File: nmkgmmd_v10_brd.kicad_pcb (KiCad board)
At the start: 2 copper layers, 85 x 69 mm, 155 parts, among them J1 CONN_01X05, J10 CONN_01X10, J14 CONN_01X10, J15 CONN_01X01, J16 CONN_01X01, J17 CONN_01X01, J18 CONN_01X01, J2 CONN_01X03, J20 CONN_01X10, J21 CONN_01X01, J22 CONN_01X01, J23 CONN_01X01, J24 CONN_01X01, J3 CONN_01X03, J4 CONN_01X04, J5 CONN_01X04, J6 CONN_01X04, J7 CONN_01X03, J8 CONN_01X03, J9 CONN_01X10, Q1 BSS138, Q10 PSMN1R0-40YLD, Q11 PSMN1R0-40YLD, Q12 PSMN1R0-40YLD, Q13 PSMN1R0-40YLD, Q14 PSMN1R0-40YLD, Q15 PSMN1R0-40YLD, Q16 PSMN1R0-40YLD, Q17 PSMN1R0-40YLD, Q18 BSS138, Q2 PSMN1R0-40YLD, Q3 PSMN1R0-40YLD, Q4 PSMN1R0-40YLD, Q5 PSMN1R0-40YLD, Q6 PSMN1R0-40YLD, Q7 PSMN1R0-40YLD, Q8 PSMN1R0-40YLD, Q9 PSMN1R0-40YLD, SW1 SKRPACE010, SW2 SW_DPDT_x2, U1 STM32F303CCTx, U2 MCP16301, U3 MCP16301, U4 A4957, U5 ACS711, U6 A4957, U7 ACS711, Y1 Crystal

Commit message: 進捗
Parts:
- moved C35 21.7 mm to (132.7, 106.7), turned to 0 degrees
- moved C33 18.5 mm to (132.7, 109.3), turned to 0 degrees
- moved C34 17.9 mm to (132.7, 108.0), turned to 0 degrees
- moved C37 2.02 mm to (132.7, 72.0)
- moved C36 1.33 mm to (132.7, 73.3)
- moved C38 0.76 mm to (132.7, 70.7)
- moved C31 0.76 mm to (126.7, 57.7)
- moved C23 0.56 mm to (124.5, 57.8)
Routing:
- net GND: track 552.0 -> 681.5 mm, vias 132 -> 162
- net V_BATT: track 209.9 -> 328.9 mm
- net (no net): track 1.40 -> 38.6 mm, vias 0 -> 10
- net +3V3: track 178.1 -> 210.4 mm, vias 7 -> 8
- net Net-(C22-Pad2): track 0.00 -> 32.2 mm, vias 0 -> 2
- net Net-(C21-Pad2): track 0.00 -> 16.9 mm, vias 0 -> 2
- net Net-(C31-Pad1): track 0.00 -> 9.49 mm, vias 0 -> 1
- net Net-(J18-Pad1): track 0.00 -> 6.72 mm
- net Net-(C20-Pad2): track 0.00 -> 2.65 mm, vias 0 -> 1

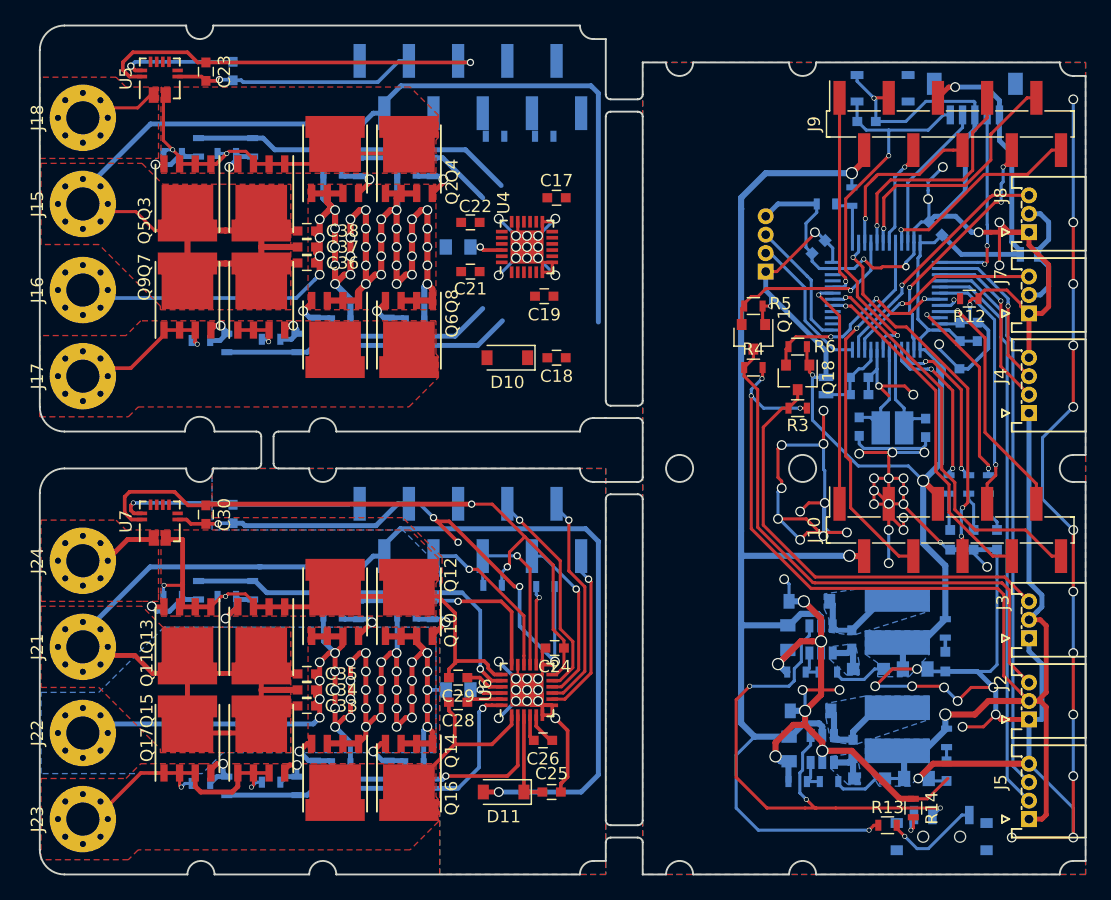
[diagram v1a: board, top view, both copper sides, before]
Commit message: 塗り忘れのviaがあったから塗った
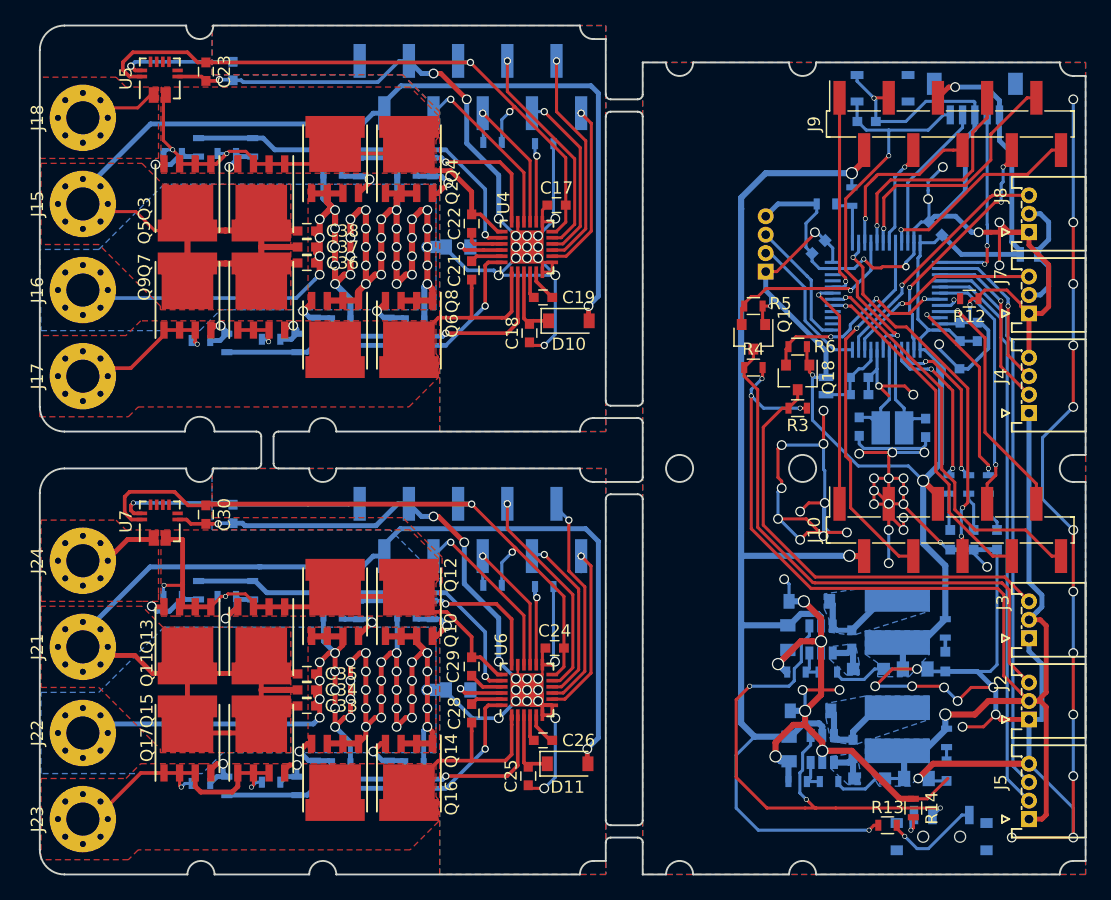
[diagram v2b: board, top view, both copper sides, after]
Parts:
- moved D10 5.83 mm to (154.0, 78.0), turned to 0 degrees
- moved D11 5.69 mm to (153.9, 114.0), turned to 0 degrees
- moved C18 2.97 mm to (150.8, 79.0), turned to 270 degrees
- moved C25 2.30 mm to (150.7, 115.0), turned to 270 degrees
- moved C28 1.42 mm to (146.1, 109.9), turned to 270 degrees
- moved C29 1.42 mm to (146.1, 106.1), turned to 90 degrees
- moved R20 0.60 mm to (152.0, 63.6)
- moved C17 0.60 mm to (153.0, 68.6)
- moved R19 0.54 mm to (147.8, 63.5)
- moved C19 0.14 mm to (151.9, 76.1)
- moved C21 0.14 mm to (146.1, 73.9), turned to 270 degrees
- moved C22 0.14 mm to (146.1, 70.1), turned to 90 degrees
- moved R38 0.10 mm to (152.0, 99.6)
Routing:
- net GND: track 681.5 -> 725.6 mm, vias 162 -> 165
- net +3V3: track 210.4 -> 229.3 mm, vias 8 -> 9
- net Net-(J14-Pad7): track 0.00 -> 18.1 mm, vias 0 -> 1
- net Net-(J14-Pad9): track 0.00 -> 18.1 mm, vias 0 -> 1
- net Net-(C21-Pad2): track 16.9 -> 33.0 mm
- net Net-(J14-Pad8): track 0.00 -> 14.5 mm, vias 0 -> 1
- net Net-(J14-Pad4): track 0.00 -> 14.4 mm, vias 0 -> 1
- net Net-(J14-Pad10): track 0.00 -> 14.3 mm, vias 0 -> 1
- net Net-(J14-Pad6): track 0.00 -> 12.8 mm, vias 0 -> 1
- net Net-(C22-Pad2): track 32.2 -> 43.4 mm
- net V_BATT: track 328.9 -> 318.8 mm, vias 4 -> 5
- net Net-(R31-Pad2): track 14.5 -> 21.1 mm, vias 0 -> 1
- net Net-(R20-Pad2): track 0.00 -> 6.43 mm, vias 0 -> 1
- net Net-(C18-Pad1): track 0.00 -> 6.04 mm
- net Net-(R22-Pad1): track 11.4 -> 16.9 mm, vias 0 -> 1
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
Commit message: via修正
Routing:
- net GND: track 725.6 -> 824.3 mm, vias 165 -> 198
- net (no net): track 38.6 -> 1.40 mm, vias 10 -> 0
- net +3V3: track 229.3 -> 231.5 mm

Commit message: 外形修正
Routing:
- net GND: track 824.3 -> 895.3 mm, vias 198 -> 214
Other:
- outline, holes or cut-outs redrawn
